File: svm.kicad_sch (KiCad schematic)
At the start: 25 parts, among them U1 INA128, U2 TL431LP, U3 TL074, U4 INA128

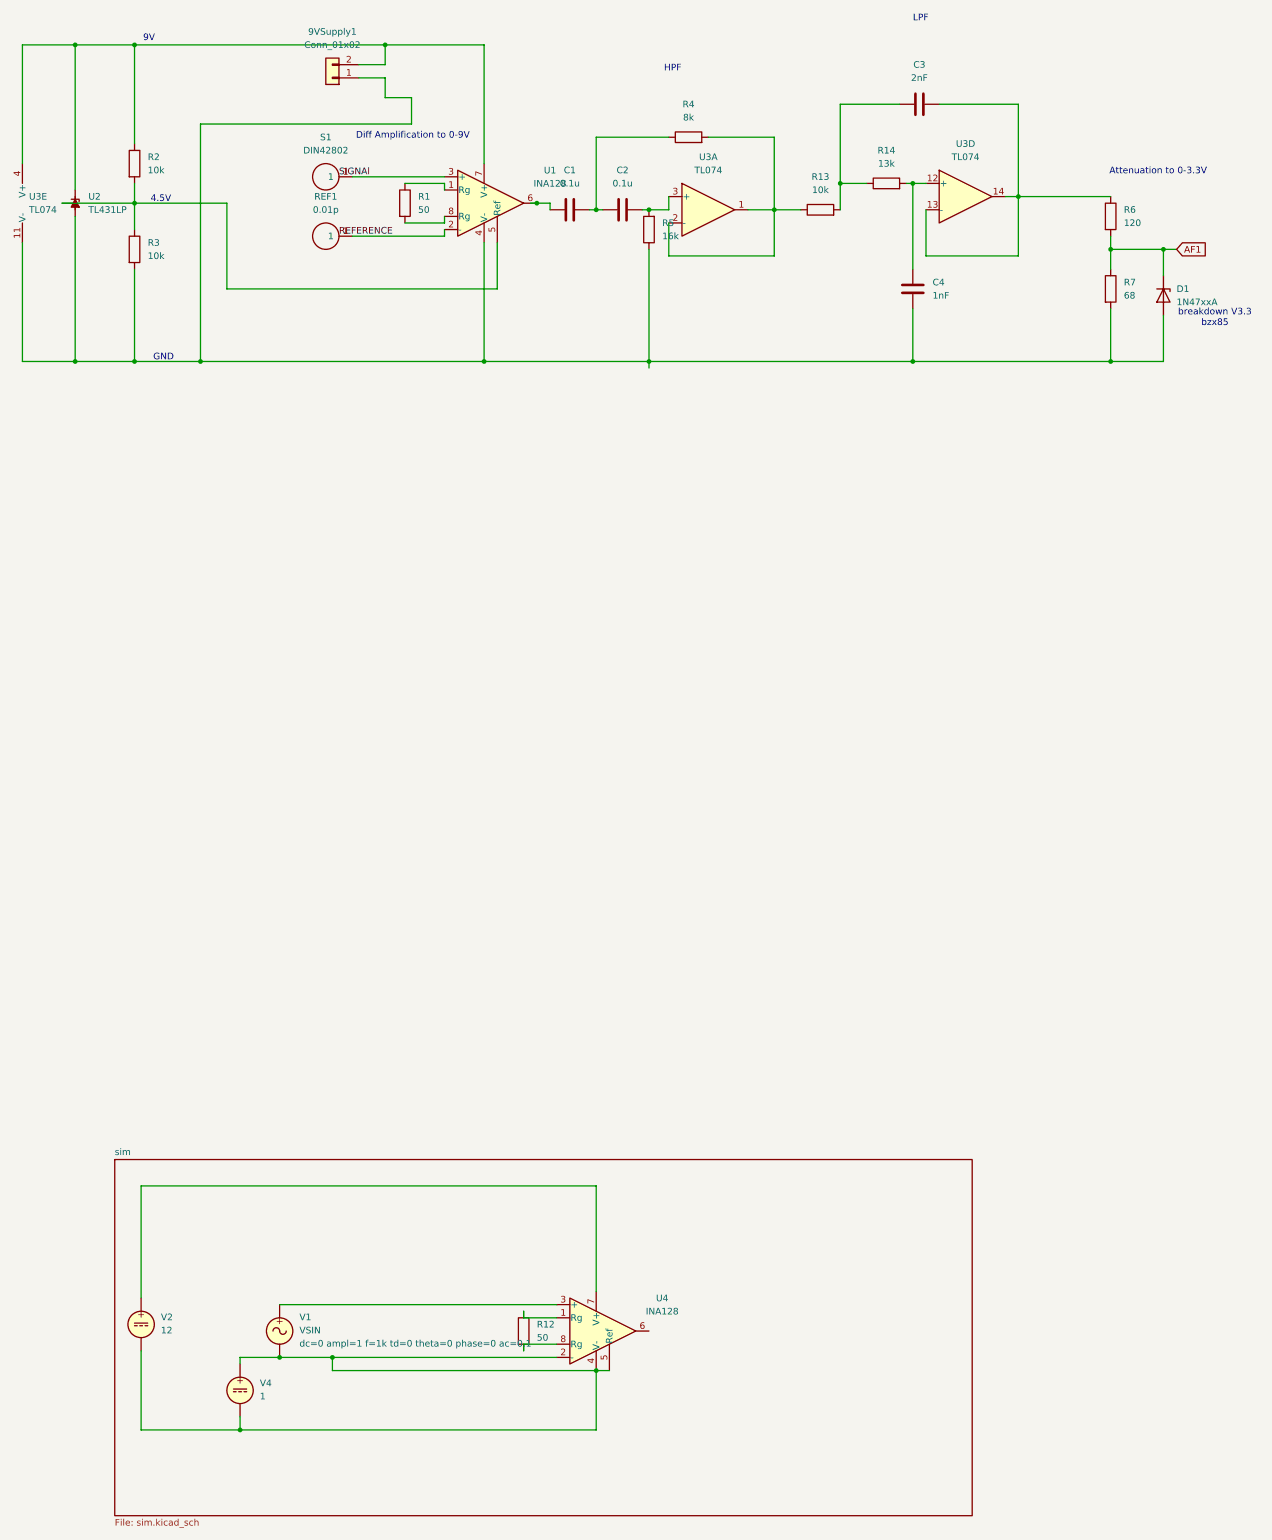
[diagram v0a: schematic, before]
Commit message: schematic, placement and routing for analog FE pcb
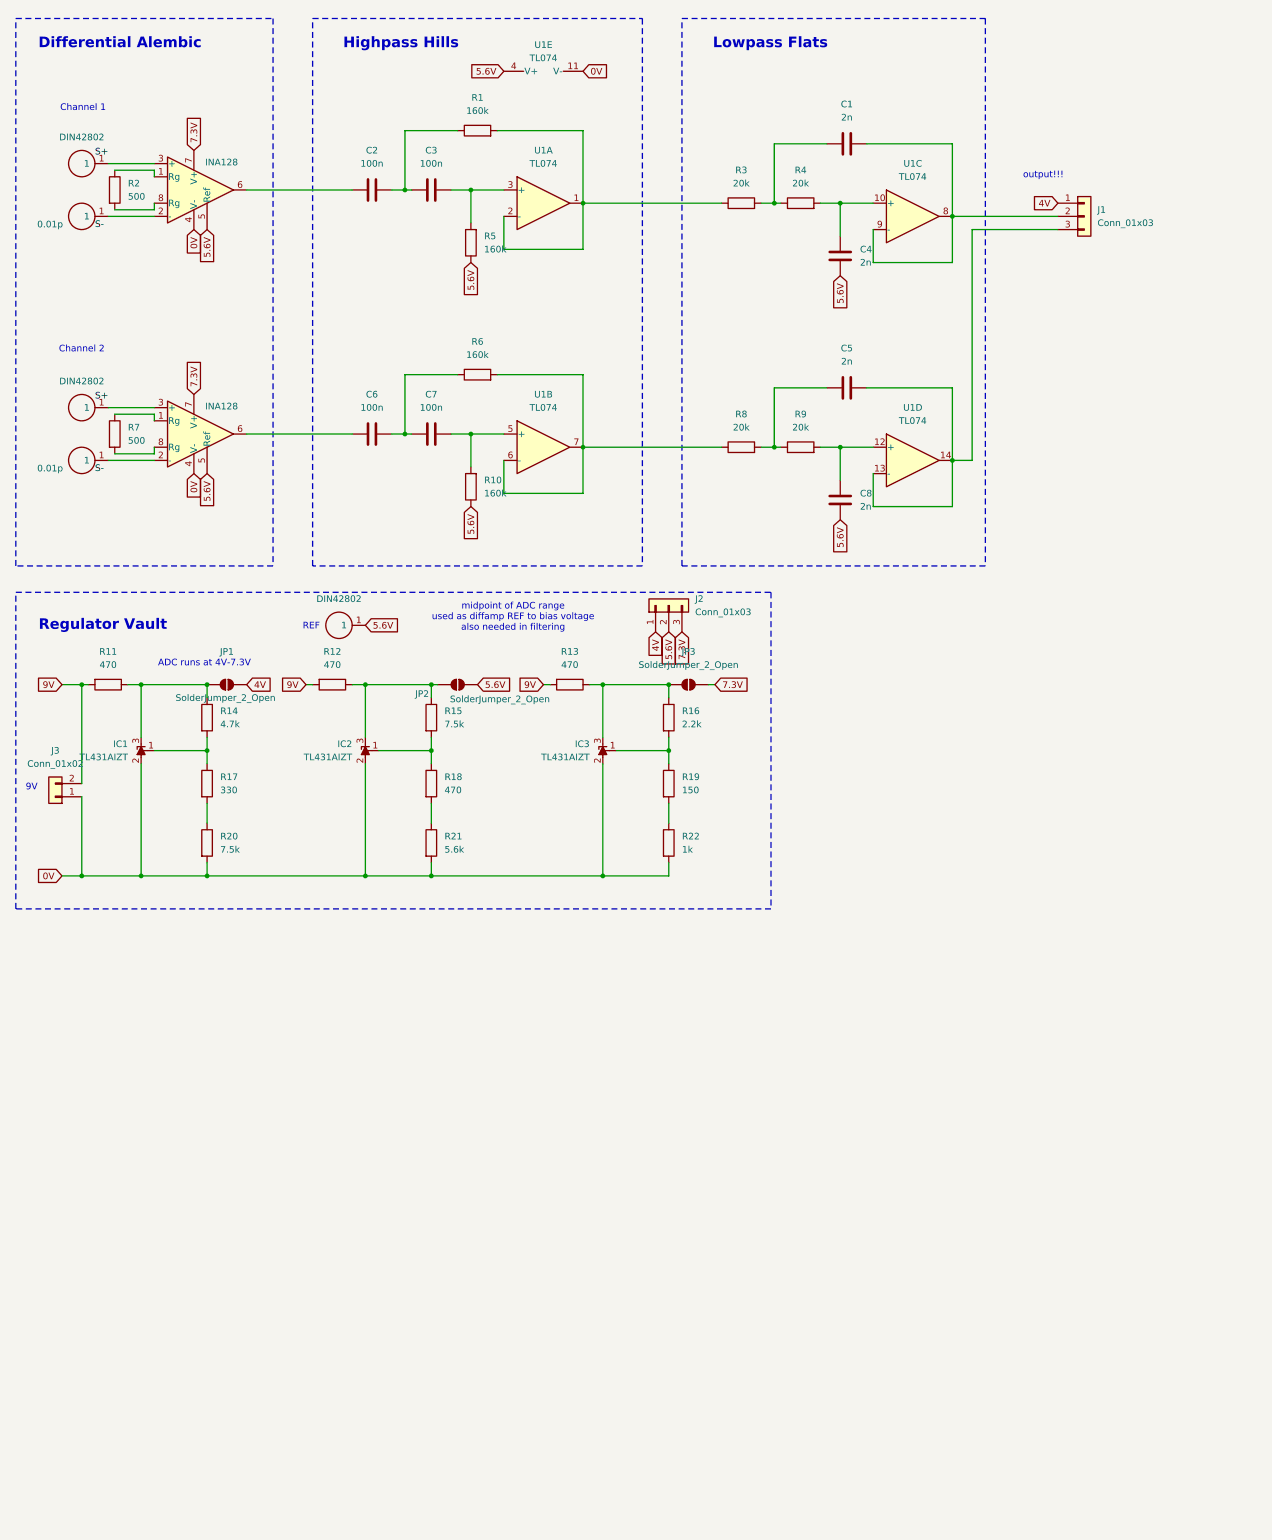
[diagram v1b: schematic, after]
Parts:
- removed 9VSupply1: Conn_01x02, symbol Connector_Generic:Conn_01x02
- removed D1: 1N47xxA, Diode_THT:D_DO-41_SOD81_P10.16mm_Horizontal, symbol Diode:1N47xxA
- removed REF1: 0.01p, lucia:EMSLIFE EE-B04, symbol lucia:DIN42802
- removed U1, U4: INA128, symbol Amplifier_Instrumentation:INA128
- removed U2: TL431LP, Package_TO_SOT_THT:TO-92_Inline, symbol Reference_Voltage:TL431LP
- removed U3: TL074, symbol Amplifier_Operational:TL074
- removed V1: VSIN, symbol Simulation_SPICE:VSIN
- removed V2: 12, symbol Simulation_SPICE:VDC
- removed V4: 1, symbol Simulation_SPICE:VDC
- added C5, C8: 2n, Capacitor_THT:C_Rect_L16.5mm_W4.7mm_P15.00mm_MKT, symbol Device:C
- added C6, C7: 100n, C_Rect_L7.2mm_W2.5mm_P5.00mm_FKS2_FKP2_MKS2_MKP2, symbol Device:C
- added IC1, IC2, IC3: TL431AIZT, lucia:TL431AIZT, symbol lucia:TL431AIZT
- added J1, J2: Conn_01x03, Connector_JST:JST_XH_B3B-XH-A_1x03_P2.50mm_Vertical, symbol Connector_Generic:Conn_01x03
- added J3: Conn_01x02, Connector_JST:JST_XH_B2B-XH-A_1x02_P2.50mm_Vertical, symbol Connector_Generic:Conn_01x02
- added JP1, JP2, JP3: SolderJumper_2_Open, Jumper:SolderJumper-2_P1.3mm_Open_RoundedPad1.0x1.5mm, symbol Jumper:SolderJumper_2_Open
- added R10: 160k, Resistor_THT:R_Axial_DIN0309_L9.0mm_D3.2mm_P12.70mm_Horizontal, symbol Device:R
- added R11, R18: 470, Resistor_THT:R_Axial_DIN0309_L9.0mm_D3.2mm_P12.70mm_Horizontal, symbol Device:R
- added R15, R20: 7.5k, Resistor_THT:R_Axial_DIN0309_L9.0mm_D3.2mm_P12.70mm_Horizontal, symbol Device:R
- added R16: 2.2k, Resistor_THT:R_Axial_DIN0309_L9.0mm_D3.2mm_P12.70mm_Horizontal, symbol Device:R
- added R17: 330, Resistor_THT:R_Axial_DIN0309_L9.0mm_D3.2mm_P12.70mm_Horizontal, symbol Device:R
- added R19: 150, Resistor_THT:R_Axial_DIN0309_L9.0mm_D3.2mm_P12.70mm_Horizontal, symbol Device:R
- added R21: 5.6k, Resistor_THT:R_Axial_DIN0309_L9.0mm_D3.2mm_P12.70mm_Horizontal, symbol Device:R
- added R22: 1k, Resistor_THT:R_Axial_DIN0309_L9.0mm_D3.2mm_P12.70mm_Horizontal, symbol Device:R
- added R8, R9: 20k, Resistor_THT:R_Axial_DIN0309_L9.0mm_D3.2mm_P12.70mm_Horizontal, symbol Device:R
- added S2, S4: 0.01p, lucia:EMSLIFE EE-B04, symbol lucia:DIN42802
- added S3, S5: DIN42802, lucia:EMSLIFE EE-B04, symbol lucia:DIN42802
- added U1: TL074, lucia:TL074CN, symbol Amplifier_Operational:TL074
- added U2, U3: INA128, lucia:INA128PA, symbol Amplifier_Instrumentation:INA128
- C1: value 0.1u -> 2n; footprint (none) -> Capacitor_THT:C_Rect_L16.5mm_W4.7mm_P15.00mm_MKT
- C2: value 0.1u -> 100n; footprint (none) -> Capacitor_THT:C_Rect_L7.2mm_W2.5mm_P5.00mm_FKS2_FKP2_MKS2_MKP2
- C3: value 2nF -> 100n; footprint (none) -> C_Rect_L7.2mm_W2.5mm_P5.00mm_FKS2_FKP2_MKS2_MKP2
- C4: value 1nF -> 2n; footprint (none) -> Capacitor_THT:C_Rect_L16.5mm_W4.7mm_P15.00mm_MKT
- R1: value 50 -> 160k; footprint (none) -> Resistor_THT:R_Axial_DIN0309_L9.0mm_D3.2mm_P12.70mm_Horizontal
- R12: value 50 -> 470; footprint (none) -> Resistor_THT:R_Axial_DIN0309_L9.0mm_D3.2mm_P12.70mm_Horizontal
- R13: value 10k -> 470; footprint (none) -> Resistor_THT:R_Axial_DIN0309_L9.0mm_D3.2mm_P12.70mm_Horizontal
- R14: value 13k -> 4.7k; footprint (none) -> Resistor_THT:R_Axial_DIN0309_L9.0mm_D3.2mm_P12.70mm_Horizontal
- R2: value 10k -> 500; footprint (none) -> Resistor_THT:R_Axial_DIN0309_L9.0mm_D3.2mm_P12.70mm_Horizontal
- R3: value 10k -> 20k; footprint (none) -> Resistor_THT:R_Axial_DIN0309_L9.0mm_D3.2mm_P12.70mm_Horizontal
- R4: value 8k -> 20k; footprint (none) -> Resistor_THT:R_Axial_DIN0309_L9.0mm_D3.2mm_P12.70mm_Horizontal
- R5: value 16k -> 160k; footprint (none) -> Resistor_THT:R_Axial_DIN0309_L9.0mm_D3.2mm_P12.70mm_Horizontal
- R6: value 120 -> 160k; footprint (none) -> Resistor_THT:R_Axial_DIN0309_L9.0mm_D3.2mm_P12.70mm_Horizontal
- R7: value 68 -> 500; footprint (none) -> Resistor_THT:R_Axial_DIN0309_L9.0mm_D3.2mm_P12.70mm_Horizontal
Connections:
- net at R1.1: now also C2.2, C3.1
- net at S1.1: now also U2.3 (+)
- net 5.6V: now reaches C4.1, R5.1
- net 5.6V: now also C8.1, J2.2 (Pin_2), JP2.2 (B), R10.1, S5.1, U1.4 (V+), U2.5 (Ref), U3.5 (Ref); no longer R3.2, R7.2
- net at R3.1: now also R1.2, U1.1, U1.2 (-); no longer R2.2
- net at C1.1: now also R3.2, R4.1
- net at R2.1: now also U2.1 (Rg)
- net at R5.2: now also C3.2, U1.3 (+); no longer C2.2
- net at C4.2: now also R4.2, U1.10 (+); no longer R14.2
- net at R6.1: now also C6.2, C7.1; no longer C3.2
- net at R12.1: now also IC2.3, JP2.1 (A), R15.1
- net 9V: now reaches R12.2
- net 9V: now also R13.2, J3.2 (Pin_2), R11.2
- net at R13.1: now also IC3.3, JP3.1 (A), R16.1; no longer R4.2
- net AF1: no longer names the net of R7.1
- net AF1: now also U3.1 (Rg); no longer R6.2
- new net: C5.1, R8.2, R9.1
- new net: C8.2, R9.2, U1.12 (+)
- new net: IC2.1, R15.2, R18.1
- new net: R18.2, R21.1
- new net: S4.1, U3.2 (-)
- new net: R7.2, U3.8 (Rg)
- new net: C7.2, R10.2, U1.5 (+)
- new net: R6.2, R8.1, U1.6 (-), U1.7
- new net: IC3.1, R16.2, R19.1
- new net: R19.2, R22.1
- new net: R17.2, R20.1
- new net: C1.2, J1.2 (Pin_2), U1.8, U1.9 (-)
- new net: C5.2, J1.3 (Pin_3), U1.13 (-), U1.14
- new net: IC1.3, JP1.1 (A), R11.1, R14.1
- new net: IC1.1, R14.2, R17.1
- new net: R2.2, U2.8 (Rg)
- new net: C6.1, U3.6
- new net: S2.1, U2.2 (-)
- new net: S3.1, U3.3 (+)
- new net: C2.1, U2.6
- new net 0V: IC1.2, IC2.2, IC3.2, J3.1 (Pin_1), R20.2, R21.2, R22.2, U1.11 (V-), U2.4 (V-), U3.4 (V-)
- new net 4V: J1.1 (Pin_1), J2.1 (Pin_1), JP1.2 (B)
- new net 7.3V: J2.3 (Pin_3), JP3.2 (B), U2.7 (V+), U3.7 (V+)
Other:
- removed sheet sim
- note added: "ADC runs at 4V-7.3V"
- note added: "Channel 1"
- note added: "Channel 2"
- note added: "Differential Alembic"
- note added: "Highpass Hills"
- note added: "Lowpass Flats"
- note added: "REF"
- note added: "Regulator Vault"
- note added: "midpoint of ADC range used as diffamp REF to bias voltage also needed in filtering"
- note added: "output!!!"
- note removed: "4.5V"
- note removed: "Attenuation to 0-3.3V"
- note removed: "Diff Amplification to 0-9V"
- note removed: "GND"
- note removed: "HPF"
- note removed: "LPF"
- note removed: "breakdown V3.3 bzx85"
